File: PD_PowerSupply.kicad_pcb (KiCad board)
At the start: 4 copper layers, 67.3 x 41.9 mm, 63 parts, among them J1 2.54mm Header, J2 Screw Terminal, Q1 STL6P3LLH6, Q2 STL6P3LLH6, U1 LM1117LD-3.3, U2 STUSB4500QTR, U3 LMR16006YQ5, U4 LTM8074IY#PBF, U5 LTC7106EDDB-1, U6 LMP92064SDE_NOPB, U8 BMD-340-A-R

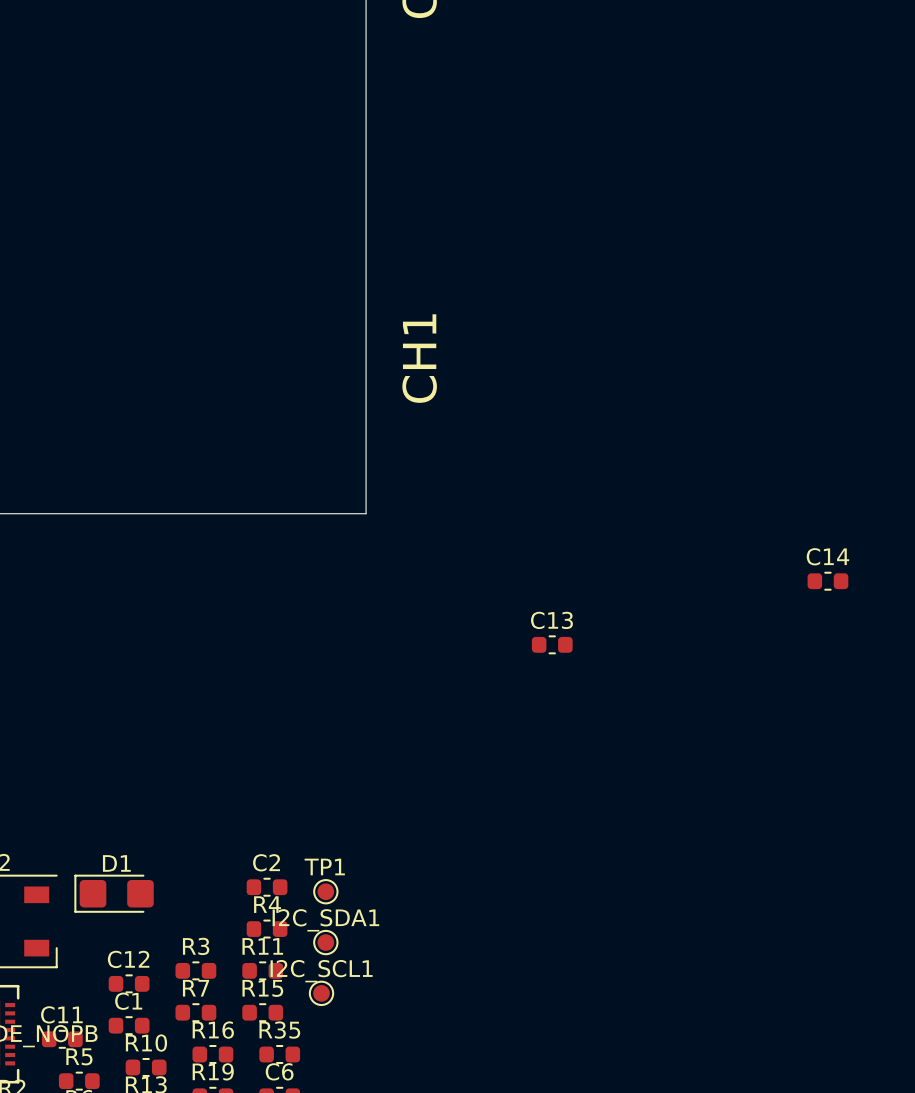
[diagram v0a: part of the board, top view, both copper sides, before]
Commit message: set feedback resistance and noted vout accuracy
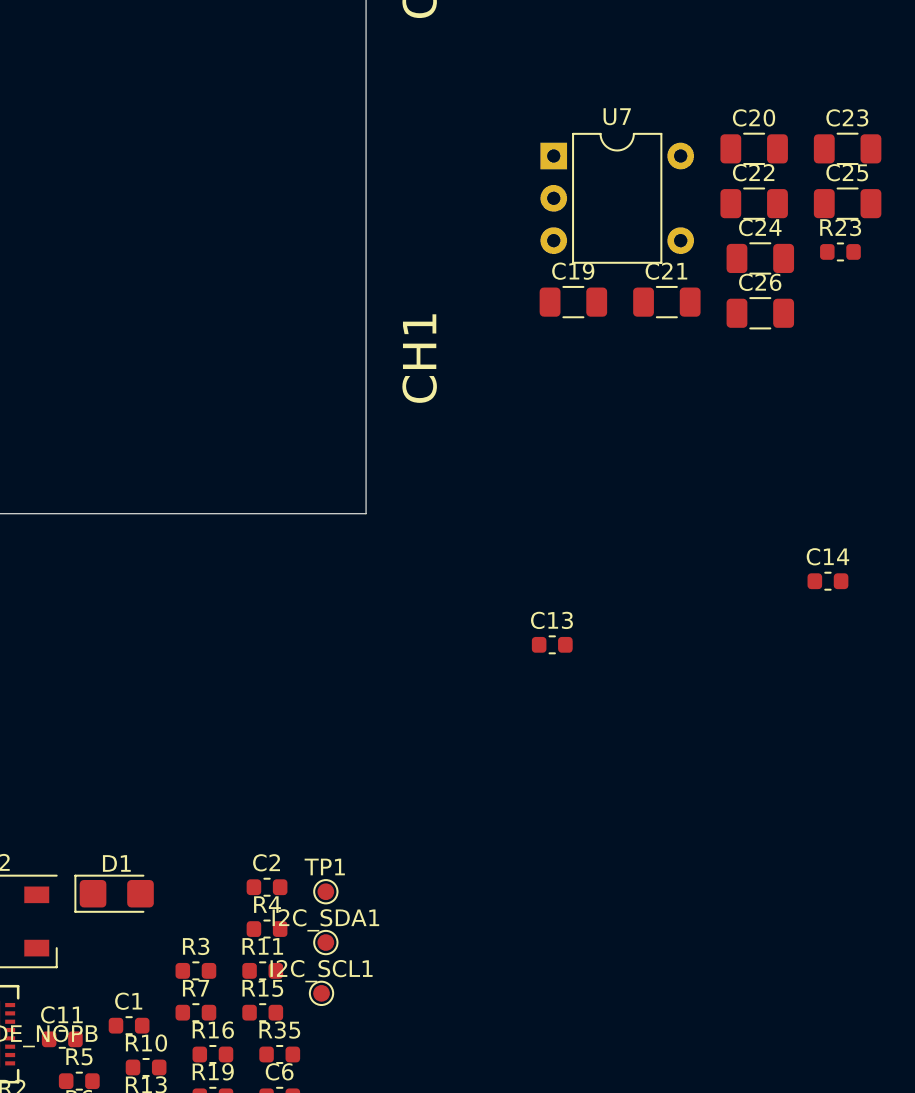
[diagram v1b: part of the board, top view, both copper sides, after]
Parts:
- removed C12: 10uF, Capacitor_SMD:C_0603_1608Metric
- added C19: 10uF, Capacitor_SMD:C_1206_3216Metric, F.Cu at (192.9, 103.3)
- added C20: 10uF, Capacitor_SMD:C_1206_3216Metric, F.Cu at (203.7, 94.1)
- added C21: 10uF, Capacitor_SMD:C_1206_3216Metric, F.Cu at (198.5, 103.3)
- added C22: 10uF, Capacitor_SMD:C_1206_3216Metric, F.Cu at (203.7, 97.3)
- added C23: 10uF, Capacitor_SMD:C_1206_3216Metric, F.Cu at (209.3, 94.1)
- added C24: 10uF, Capacitor_SMD:C_1206_3216Metric, F.Cu at (204.1, 100.6)
- added C25: 10uF, Capacitor_SMD:C_1206_3216Metric, F.Cu at (209.3, 97.3)
- added C26: 10uF, Capacitor_SMD:C_1206_3216Metric, F.Cu at (204.1, 103.9)
- added R23: 1.1K, Resistor_SMD:R_0603_1608Metric, F.Cu at (208.9, 100.2)
- added U7: TLP3542, Package_DIP:DIP-5-6_W7.62mm, F.Cu at (191.7, 94.5)
- R17: value div1 -> 12K
- R19: value div2 -> 2.2K
- U4: value LTM8074IY#PBF -> LTM8074IY
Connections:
- C6 pad 1: +3V3 -> +5V
- D2 pad 1: +3V3 -> +5V
- U4 pad E1: /VOUT -> /VOUT_PRE_SWITCH
- U4 pad E2: /VOUT -> /VOUT_PRE_SWITCH
- U8 pad 32: (no net) -> /OUTPUT_EN

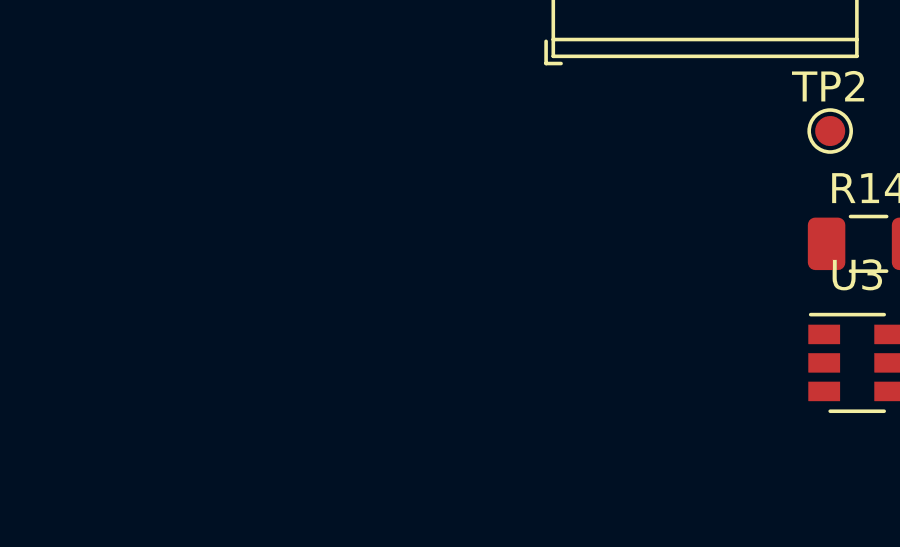
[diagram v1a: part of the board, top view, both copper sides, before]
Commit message: Added in capacitor for diode protection
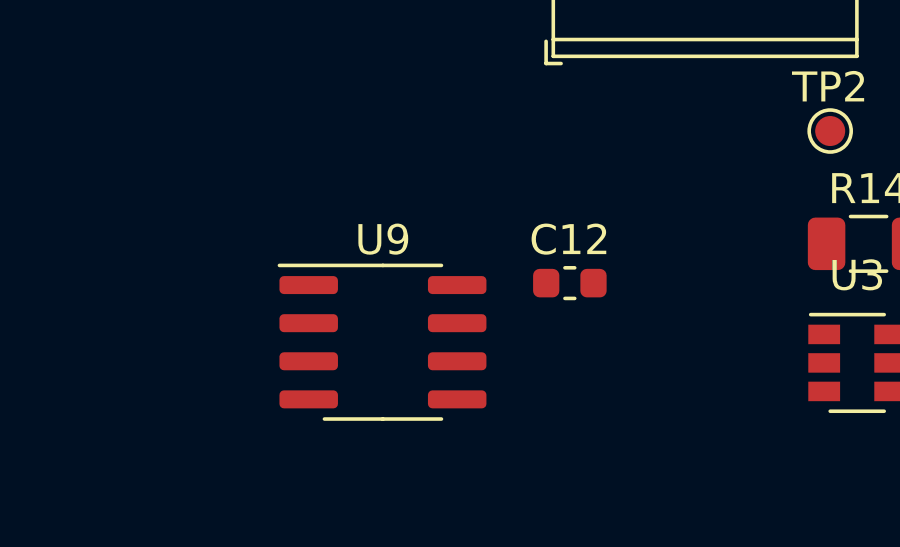
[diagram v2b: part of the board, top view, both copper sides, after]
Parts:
- added C12: .1uF, Capacitor_SMD:C_0603_1608Metric, F.Cu at (135.2, 155.6)
- added U9: USB6B1, Package_SO:SOIC-8_3.9x4.9mm_P1.27mm, F.Cu at (129.0, 157.6)
- C9: value C -> .1uF
- R12: value FEEDBACK -> 47K
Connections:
- USB1 pad A6: Net-(U8-Pad68) -> Net-(U9-Pad3)
- USB1 pad A7: Net-(U8-Pad67) -> Net-(U9-Pad2)
- USB1 pad B6: Net-(U8-Pad68) -> Net-(U9-Pad3)
- USB1 pad B7: Net-(U8-Pad67) -> Net-(U9-Pad2)
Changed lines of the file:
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@@
     (tracks 32)
     (zones 0)
-    (modules 72)
-    (nets 68)
+    (modules 74)
+    (nets 70)
   )
   (page A4)
@@
   (net 66 "Net-(U7-Pad3)")
   (net 67 /OUTPUT_EN)
+  (net 68 "Net-(U9-Pad3)")
+  (net 69 "Net-(U9-Pad2)")
   (net_class Default "This is the default net class."
     (clearance 0.2)
@@
     (add_net "Net-(U8-Pad67)")
     (add_net "Net-(U8-Pad68)")
+    (add_net "Net-(U9-Pad2)")
+    (add_net "Net-(U9-Pad3)")
     (add_net "Net-(USB1-PadA8)")
     (add_net "Net-(USB1-PadB8)")
   )
+  (module Package_SO:SOIC-8_3.9x4.9mm_P1.27mm (layer F.Cu)
+    (at 128.968 157.554)
+    (descr "SOIC, 8 Pin (JEDEC MS-012AA, https://www.analog.com/media/en/package-pcb-resources/package/pkg_pdf/soic_narrow-r/r_8.pdf), generated with kicad-footprint-generator ipc_gullwing_generator.py")
+    (tags "SOIC SO")
+    (attr smd)
+    (fp_text reference U9 (at 0 -3.4) (layer F.SilkS)
+      (effects (font (size 1 1) (thickness 0.15)))
+    )
+    (fp_text value USB6B1 (at 0 3.4) (layer F.Fab)
+      (effects (font (size 1 1) (thickness 0.15)))
+    )
+    (fp_text user %R (at 0 0) (layer F.Fab)
+      (effects (font (size 0.98 0.98) (thickness 0.15)))
+    )
+    (fp_line (start 3.7 -2.7) (end -3.7 -2.7) (layer F.CrtYd) (width 0.05))
+    (fp_line (start 3.7 2.7) (end 3.7 -2.7) (layer F.CrtYd) (width 0.05))
+    (fp_line (start -3.7 2.7) (end 3.7 2.7) (layer F.CrtYd) (width 0.05))
+    (fp_line (start -3.7 -2.7) (end -3.7 2.7) (layer F.CrtYd) (width 0.05))
+    (fp_line (start -1.95 -1.475) (end -0.975 -2.45) (layer F.Fab) (width 0.1))
+    (fp_line (start -1.95 2.45) (end -1.95 -1.475) (layer F.Fab) (width 0.1))
+    (fp_line (start 1.95 2.45) (end -1.95 2.45) (layer F.Fab) (width 0.1))
+    (fp_line (start 1.95 -2.45) (end 1.95 2.45) (layer F.Fab) (width 0.1))
+    (fp_line (start -0.975 -2.45) (end 1.95 -2.45) (layer F.Fab) (width 0.1))
+    (fp_line (start 0 -2.56) (end -3.45 -2.56) (layer F.SilkS) (width 0.12))
+    (fp_line (start 0 -2.56) (end 1.95 -2.56) (layer F.SilkS) (width 0.12))
+    (fp_line (start 0 2.56) (end -1.95 2.56) (layer F.SilkS) (width 0.12))
+    (fp_line (start 0 2.56) (end 1.95 2.56) (layer F.SilkS) (width 0.12))
+    (pad 8 smd roundrect (at 2.475 -1.905) (size 1.95 0.6) (layers F.Cu F.Paste F.Mask) (roundrect_rratio 0.25)
+      (net 41 +5V))
+    (pad 7 smd roundrect (at 2.475 -0.635) (size 1.95 0.6) (layers F.Cu F.Paste F.Mask) (roundrect_rratio 0.25)
+      (net 50 "Net-(U8-Pad67)"))
+    (pad 6 smd roundrect (at 2.475 0.635) (size 1.95 0.6) (layers F.Cu F.Paste F.Mask) (roundrect_rratio 0.25)
+      (net 49 "Net-(U8-Pad68)"))
+    (pad 5 smd roundrect (at 2.475 1.905) (size 1.95 0.6) (layers F.Cu F.Paste F.Mask) (roundrect_rratio 0.25)
+      (net 3 GND))
+    (pad 4 smd roundrect (at -2.475 1.905) (size 1.95 0.6) (layers F.Cu F.Paste F.Mask) (roundrect_rratio 0.25)
+      (net 3 GND))
+    (pad 3 smd roundrect (at -2.475 0.635) (size 1.95 0.6) (layers F.Cu F.Paste F.Mask) (roundrect_rratio 0.25)
+      (net 68 "Net-(U9-Pad3)"))
+    (pad 2 smd roundrect (at -2.475 -0.635) (size 1.95 0.6) (layers F.Cu F.Paste F.Mask) (roundrect_rratio 0.25)
+      (net 69 "Net-(U9-Pad2)"))
+    (pad 1 smd roundrect (at -2.475 -1.905) (size 1.95 0.6) (layers F.Cu F.Paste F.Mask) (roundrect_rratio 0.25)
+      (net 41 +5V))
+    (model ${KISYS3DMOD}/Package_SO.3dshapes/SOIC-8_3.9x4.9mm_P1.27mm.wrl
+      (at (xyz 0 0 0))
+      (scale (xyz 1 1 1))
+      (rotate (xyz 0 0 0))
+    )
+  )
+  (module Capacitor_SMD:C_0603_1608Metric (layer F.Cu)
+    (at 135.198 155.584)
+    (descr "Capacitor SMD 0603 (1608 Metric), square (rectangular) end terminal, IPC_7351 nominal, (Body size source: http://www.tortai-tech.com/upload/download/2011102023233369053.pdf), generated with kicad-footprint-generator")
+    (tags capacitor)
+    (attr smd)
+    (fp_text reference C12 (at 0 -1.43) (layer F.SilkS)
+      (effects (font (size 1 1) (thickness 0.15)))
+    )
+    (fp_text value .1uF (at 0 1.43) (layer F.Fab)
+      (effects (font (size 1 1) (thickness 0.15)))
+    )
+    (fp_text user %R (at 0 0) (layer F.Fab)
+      (effects (font (size 0.4 0.4) (thickness 0.06)))
+    )
+    (fp_line (start 1.48 0.73) (end -1.48 0.73) (layer F.CrtYd) (width 0.05))
+    (fp_line (start 1.48 -0.73) (end 1.48 0.73) (layer F.CrtYd) (width 0.05))
+    (fp_line (start -1.48 -0.73) (end 1.48 -0.73) (layer F.CrtYd) (width 0.05))
+    (fp_line (start -1.48 0.73) (end -1.48 -0.73) (layer F.CrtYd) (width 0.05))
+    (fp_line (start -0.162779 0.51) (end 0.162779 0.51) (layer F.SilkS) (width 0.12))
+    (fp_line (start -0.162779 -0.51) (end 0.162779 -0.51) (layer F.SilkS) (width 0.12))
+    (fp_line (start 0.8 0.4) (end -0.8 0.4) (layer F.Fab) (width 0.1))
+    (fp_line (start 0.8 -0.4) (end 0.8 0.4) (layer F.Fab) (width 0.1))
+    (fp_line (start -0.8 -0.4) (end 0.8 -0.4) (layer F.Fab) (width 0.1))
+    (fp_line (start -0.8 0.4) (end -0.8 -0.4) (layer F.Fab) (width 0.1))
+    (pad 2 smd roundrect (at 0.7875 0) (size 0.875 0.95) (layers F.Cu F.Paste F.Mask) (roundrect_rratio 0.25)
+      (net 3 GND))
+    (pad 1 smd roundrect (at -0.7875 0) (size 0.875 0.95) (layers F.Cu F.Paste F.Mask) (roundrect_rratio 0.25)
+      (net 41 +5V))
+    (model ${KISYS3DMOD}/Capacitor_SMD.3dshapes/C_0603_1608Metric.wrl
+      (at (xyz 0 0 0))
+      (scale (xyz 1 1 1))
+      (rotate (xyz 0 0 0))
+    )
+  )
   (module Package_DIP:DIP-5-6_W7.62mm (layer F.Cu)
     (at 191.676 94.49)
@@
       (effects (font (size 1 1) (thickness 0.15)))
     )
-    (fp_text value FEEDBACK (at 0 1.43) (layer F.Fab)
+    (fp_text value 47K (at 0 1.43) (layer F.Fab)
       (effects (font (size 1 1) (thickness 0.15)))
     )
@@
       (effects (font (size 1 1) (thickness 0.15)))
     )
-    (fp_text value C (at 0 1.43) (layer F.Fab)
+    (fp_text value .1uF (at 0 1.43) (layer F.Fab)
       (effects (font (size 1 1) (thickness 0.15)))
     )
@@
       (net 14 "Net-(USB1-PadB8)"))
     (pad B7 thru_hole circle (at -0.425 -2.675 270) (size 0.65 0.65) (drill 0.4) (layers *.Cu *.Mask)
-      (net 50 "Net-(U8-Pad67)"))
+      (net 69 "Net-(U9-Pad2)"))
     (pad B6 thru_hole circle (at 0.425 -2.675 270) (size 0.65 0.65) (drill 0.4) (layers *.Cu *.Mask)
-      (net 49 "Net-(U8-Pad68)"))
+      (net 68 "Net-(U9-Pad3)"))
     (pad B5 thru_hole circle (at 1.275 -2.675 270) (size 0.65 0.65) (drill 0.4) (layers *.Cu *.Mask)
       (net 34 "Net-(U2-Pad4)"))
@@
       (net 15 "Net-(USB1-PadA8)"))
     (pad A7 thru_hole circle (at 0.425 -4.025 270) (size 0.65 0.65) (drill 0.4) (layers *.Cu *.Mask)
-      (net 50 "Net-(U8-Pad67)"))
+      (net 69 "Net-(U9-Pad2)"))
     (pad A6 thru_hole circle (at -0.425 -4.025 270) (size 0.65 0.65) (drill 0.4) (layers *.Cu *.Mask)
-      (net 49 "Net-(U8-Pad68)"))
+      (net 68 "Net-(U9-Pad3)"))
     (pad A5 thru_hole circle (at -1.275 -4.025 270) (size 0.65 0.65) (drill 0.4) (layers *.Cu *.Mask)
       (net 35 "Net-(U2-Pad1)"))

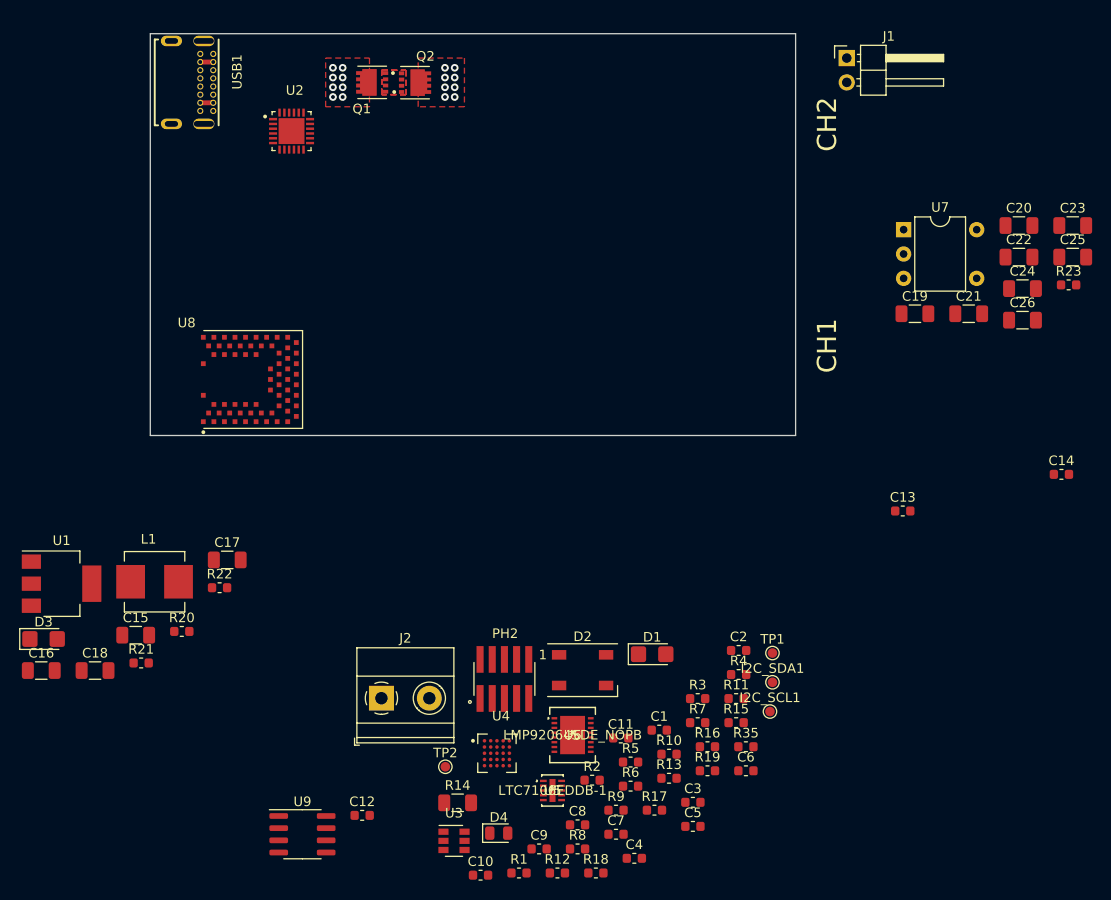
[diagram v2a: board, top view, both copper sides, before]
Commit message: Started routing process, swapped out photorelay for an SMD alternative
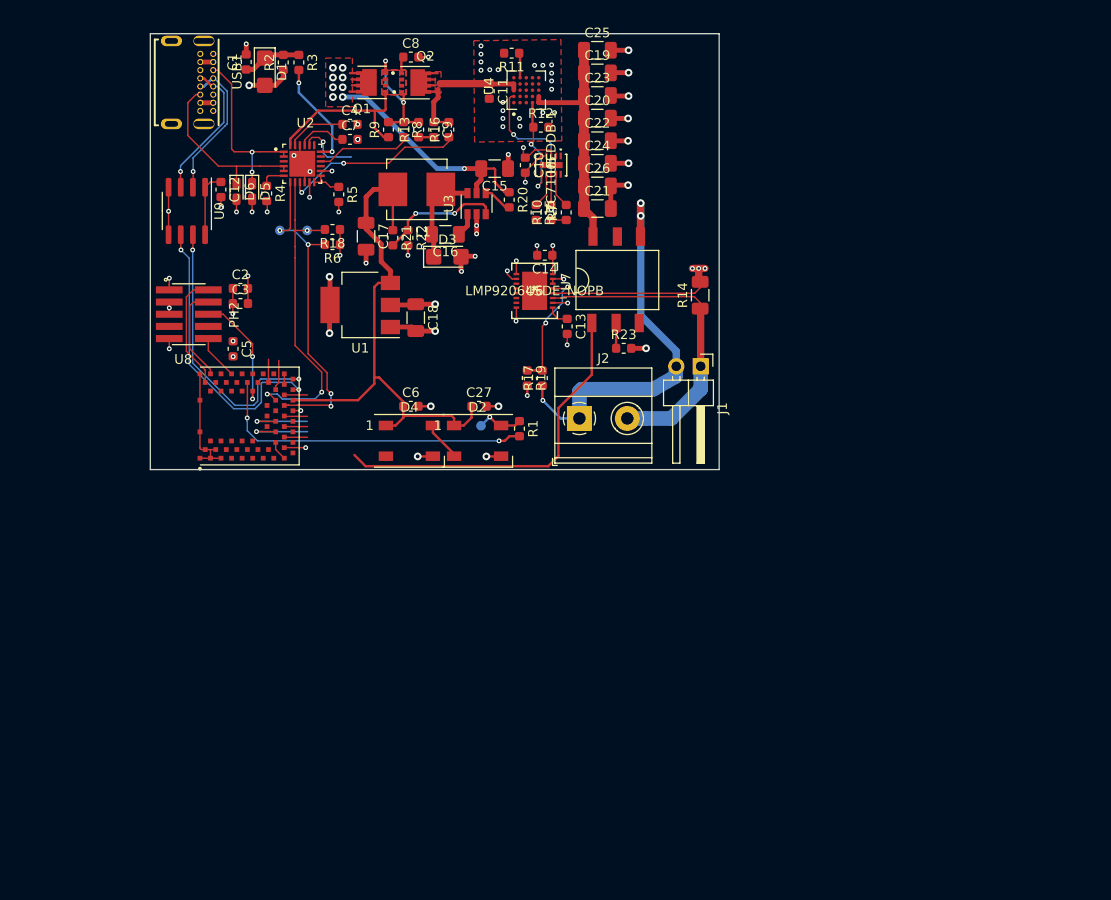
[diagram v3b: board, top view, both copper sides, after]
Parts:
- removed R35: 300, Resistor_SMD:R_0603_1608Metric
- removed TP1, TP2: TestPoint, TestPoint:TestPoint_Pad_D1.0mm
- added C27: .1uF, Capacitor_SMD:C_0603_1608Metric, F.Cu at (147.4, 112.9)
- added D5: D_Schottky, Diode_SMD:D_0603_1608Metric_Castellated, F.Cu at (123.7, 90.5)
- added D6: D_Schottky, Diode_SMD:D_0603_1608Metric_Castellated, F.Cu at (122.1, 90.5)
- added TP3: TestPoint, TestPoint:TestPoint_Pad_D1.0mm, B.Cu at (147.6, 114.9)
- D4: value BLUE 0805 -> WS2812B; footprint LED_SMD:LED_0805_2012Metric -> LED_SMD:LED_WS2812B_PLCC4_5.0x5.0mm_P3.2mm
- I2C_SCL1, I2C_SDA1: moved to B.Cu
- U7: value TLP3542 -> AQV252GAX; footprint Package_DIP:DIP-5-6_W7.62mm -> AQV252GAX:SOP6
- moved C4 82.1 mm to (133.9, 83.5)
- moved C8 82.0 mm to (140.3, 76.5)
- moved C1 81.9 mm to (123.1, 77.0), turned to 90 degrees
- moved R2 81.5 mm to (127.0, 77.0), turned to 90 degrees
- moved R3 78.3 mm to (128.6, 77.0), turned to 270 degrees
- moved R12 77.8 mm to (153.8, 83.8)
- moved C7 77.6 mm to (133.9, 85.1)
- moved R8 77.2 mm to (139.5, 84.1), turned to 270 degrees
- moved C9 75.8 mm to (142.7, 84.1), turned to 270 degrees
- moved R9 74.8 mm to (137.9, 84.1), turned to 90 degrees
- moved C10 74.2 mm to (152.2, 87.8), turned to 270 degrees
- moved D1 73.0 mm to (125.0, 78.0), turned to 270 degrees
- moved R18 72.5 mm to (132.1, 94.5), turned to 180 degrees
- moved R13 72.5 mm to (141.1, 84.1), turned to 90 degrees
- moved I2C_SCL1 71.6 mm to (126.6, 94.6)
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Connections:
- D4 pad 1: Net-(D4-Pad1) -> +5V
- U8 pad 24: Net-(D4-Pad2) -> Net-(U8-Pad24)
- U9 pad 6: Net-(U8-Pad68) -> Net-(U8-Pad67)
- U9 pad 7: Net-(U8-Pad67) -> Net-(U8-Pad68)
- USB1 pad A6: Net-(U9-Pad3) -> Net-(U9-Pad2)
- USB1 pad A7: Net-(U9-Pad2) -> Net-(U9-Pad3)
- USB1 pad B6: Net-(U9-Pad3) -> Net-(U9-Pad2)
- USB1 pad B7: Net-(U9-Pad2) -> Net-(U9-Pad3)
- USB1 pad P1: GND -> Net-(USB1-PadP1)
- USB1 pad P2: GND -> Net-(USB1-PadP1)
- USB1 pad P3: GND -> Net-(USB1-PadP1)
- USB1 pad P4: GND -> Net-(USB1-PadP1)
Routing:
- net GND: track 17.7 -> 104.3 mm, vias 0 -> 68
- net +5V: track 0.00 -> 62.8 mm
- net /VOUT: track 0.00 -> 43.7 mm, vias 0 -> 3
- net /OUTPUT_EN: track 0.00 -> 40.2 mm
- net /VUSB_RAW: track 7.83 -> 46.9 mm, vias 8 -> 10
- net /I2C_SCL: track 0.00 -> 34.3 mm, vias 0 -> 4
- net Net-(R1-Pad2): track 0.00 -> 34.1 mm, vias 0 -> 2
- net Net-(J1-Pad1): track 0.00 -> 33.7 mm
- net /I2C_SDA: track 0.00 -> 33.6 mm, vias 0 -> 3
- net +3V3: track 0.00 -> 31.1 mm, vias 0 -> 12
- net Net-(U8-Pad67): track 0.00 -> 30.5 mm, vias 0 -> 2
- net Net-(U8-Pad68): track 0.00 -> 29.2 mm, vias 0 -> 2
- net /VOUT_PRE_SWITCH: track 0.00 -> 25.2 mm
- net /vSINK: track 0.69 -> 23.1 mm, vias 8 -> 0
- net Net-(R16-Pad1): track 0.00 -> 19.2 mm, vias 0 -> 2
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- added copper zone on In1.Cu, net +3V3
- added copper zone on F.Cu, net GND
- added copper zone on In2.Cu, net GND
- removed copper zone on In2.Cu, net +3V3
- removed copper zone on In1.Cu, net /vSINK
- removed copper zone on In1.Cu, net GND
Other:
- board size 67.3 x 41.9 mm -> 59.3 x 45.5 mm
- board text removed: "CH1"
- board text removed: "CH2"
